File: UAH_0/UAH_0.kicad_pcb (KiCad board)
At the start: 2 copper layers, 100 x 100 mm, 30 parts, among them X1 Check_point, X2 Check_point, X3 LOGO_NIKITOS_19х7, X5 Клеммник_х2_KLS2-300-5.00-02P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

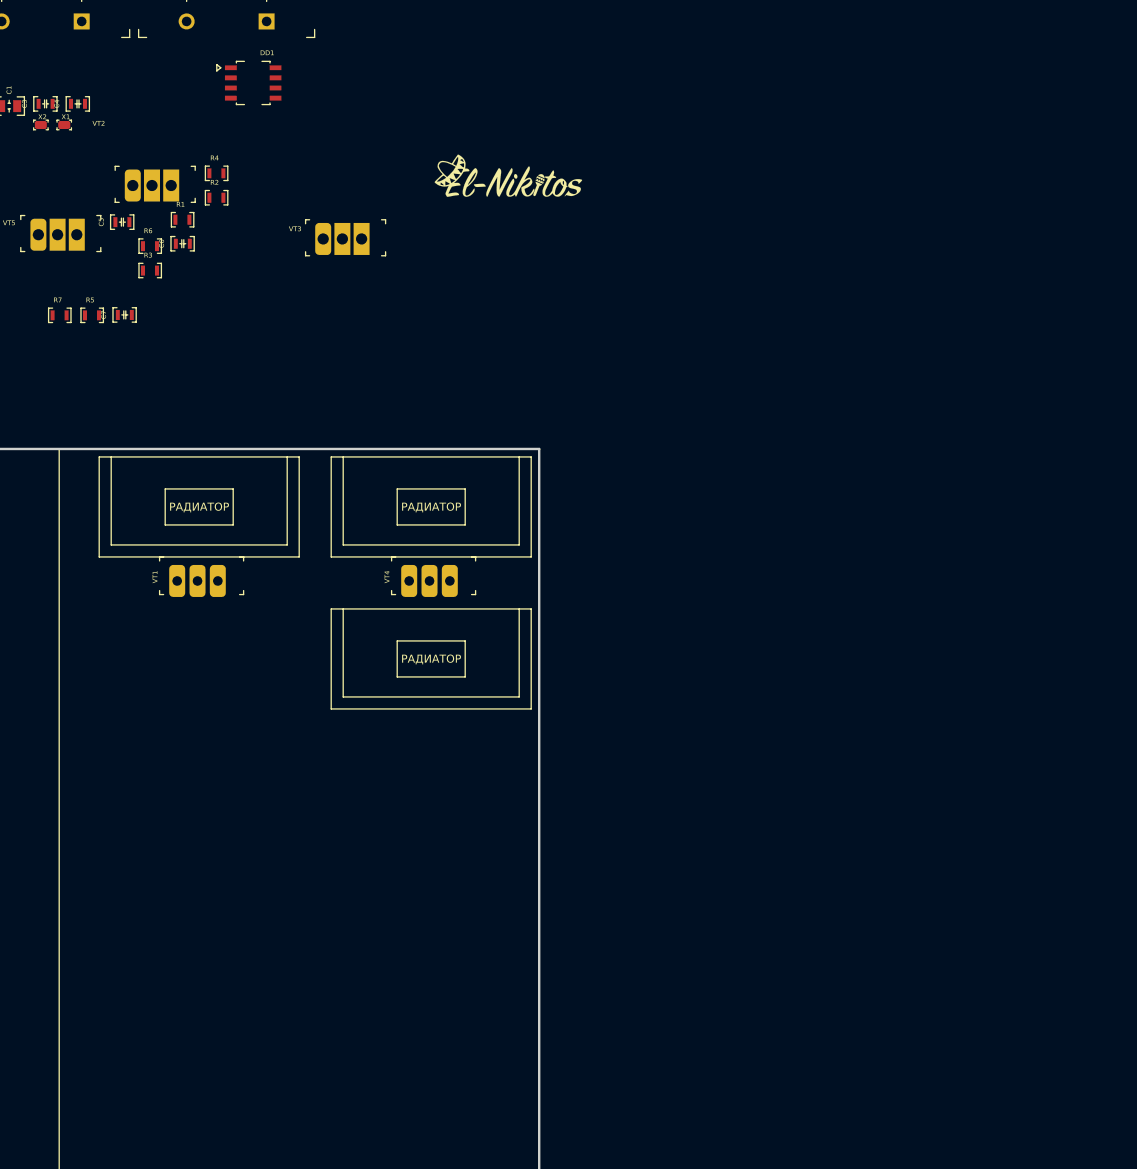
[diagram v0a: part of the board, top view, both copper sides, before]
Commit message: обновлена схема управления движками
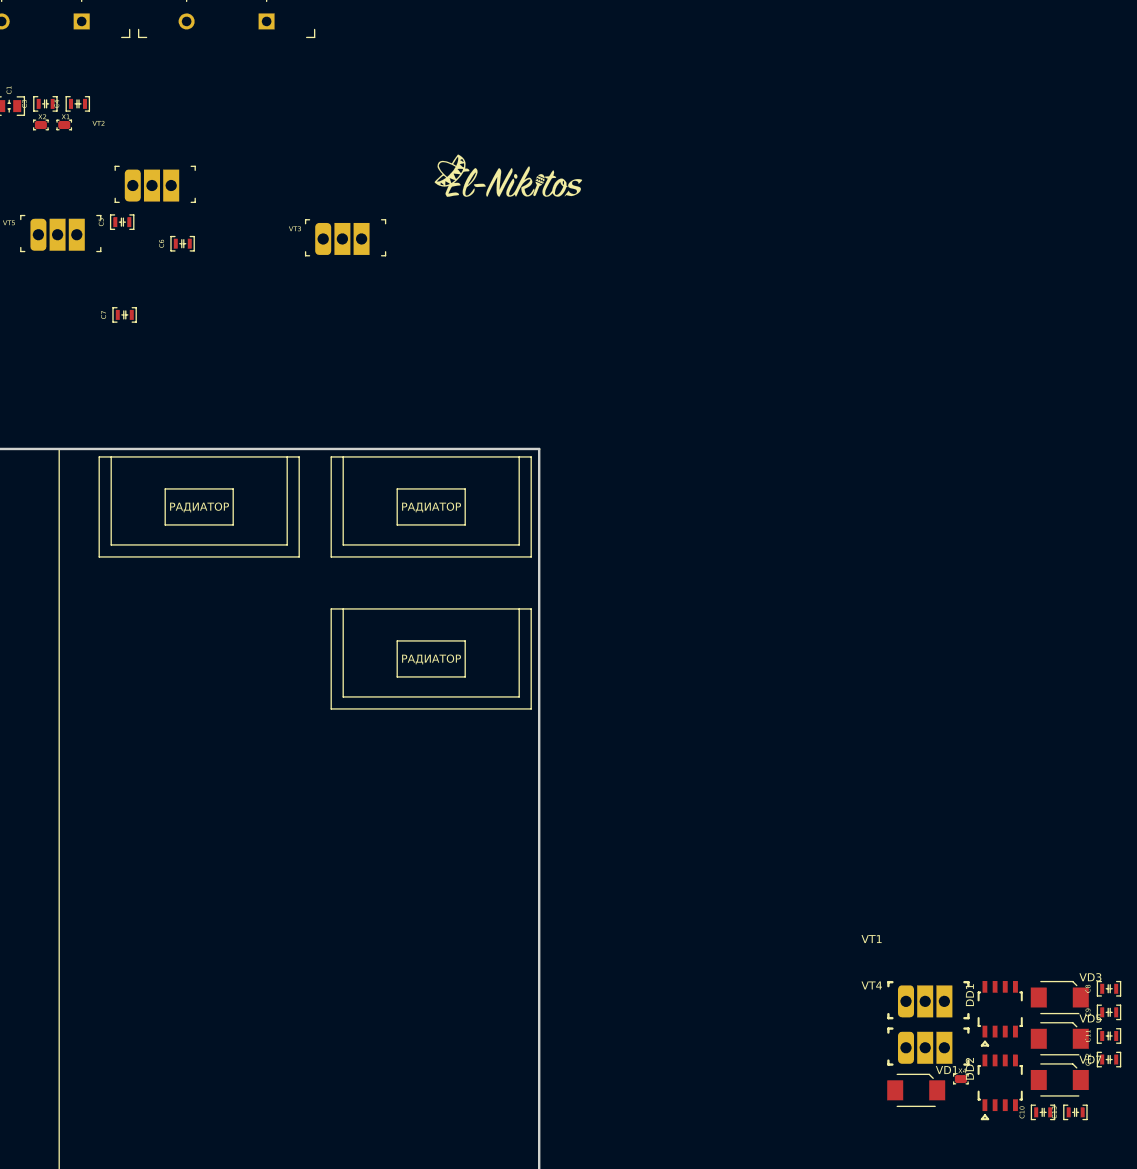
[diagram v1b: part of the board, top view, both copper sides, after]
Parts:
- removed R1, R2, R6, R7: Резистор_10_кОм±5%_0,1Вт, MOTOR_RLC:Резистор_SMD_0603-0,075_Вт
- removed R3, R4, R5: Резистор_470_Ом±5%_0,1Вт, MOTOR_RLC:Резистор_SMD_0603-0,075_Вт
- added C10: Конденсатор_16В_0.1_мкФ+-10проц., MOTOR_RLC:Конденсатор_SMD_К10-83(0603), F.Cu at (212.1, 132.9)
- added C11: Конденсатор_16В_0.1_мкФ+-10проц., MOTOR_RLC:Конденсатор_SMD_К10-83(0603), F.Cu at (220.4, 123.4)
- added C12: Конденсатор_16В_0.1_мкФ+-10проц., MOTOR_RLC:Конденсатор_SMD_К10-83(0603), F.Cu at (220.4, 126.3)
- added C13: Конденсатор_16В_0.1_мкФ+-10проц., MOTOR_RLC:Конденсатор_SMD_К10-83(0603), F.Cu at (216.2, 132.9)
- added C8: Конденсатор_16В_0.1_мкФ+-10проц., MOTOR_RLC:Конденсатор_SMD_К10-83(0603), F.Cu at (220.4, 117.5)
- added C9: Конденсатор_16В_0.1_мкФ+-10проц., MOTOR_RLC:Конденсатор_SMD_К10-83(0603), F.Cu at (220.4, 120.4)
- added DD2: Драйвер_FET-IGBT_IR2103STRPBF, N_DD:SO-8, F.Cu at (207.6, 129.2)
- added VD1: Диод_шоттки_SK16, N_VD_HL:Диод_SMB, F.Cu at (194.8, 130.2)
- added VD3: Диод_шоттки_SK16, N_VD_HL:Диод_SMB, F.Cu at (212.7, 118.6)
- added VD5: Диод_шоттки_SK16, N_VD_HL:Диод_SMB, F.Cu at (212.7, 123.7)
- added VD7: Диод_шоттки_SK16, N_VD_HL:Диод_SMB, F.Cu at (212.7, 128.9)
- added X4: Check_point, N_X:Пробник, F.Cu at (202.7, 128.8)
- VT1, VT4: value MOSFET_P-канал_IRF4905PBF -> MOSFET_N-канал_AUIRF3205Z; footprint N_VD_HL:Транзистор_P_IRF9Z24NPBF -> N_VD_HL:Транзистор_N_STP10NK60Z
- moved DD1 148.7 mm to (207.6, 120.0), turned to 0 degrees
- moved VT1 105.2 mm to (195.9, 119.1)
- moved VT4 85.2 mm to (195.9, 124.9)
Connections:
- C5 pad 1: Net-(C5-Pad1) -> /PWR_COMMUTATION/12V
- C7 pad 1: Net-(C7-Pad1) -> /PWR_COMMUTATION/12V
- DD1 pad 1: Net-(DD1-Pad1) -> /PWR_COMMUTATION/15V
- DD1 pad 2: Net-(DD1-Pad2) -> /PWR_COMMUTATION/MODE_1
- DD1 pad 3: Net-(DD1-Pad3) -> /PWR_COMMUTATION/MODE_1
- DD1 pad 4: Net-(DD1-Pad4) -> /PWR_COMMUTATION/GND
- DD1 pad 5: Net-(DD1-Pad5) -> /PWR_COMMUTATION/MODE_1_L
- DD1 pad 6: Net-(DD1-Pad6) -> /PWR_COMMUTATION/OUT_2
- DD1 pad 7: Net-(DD1-Pad7) -> /PWR_COMMUTATION/MODE_1_H
- DD1 pad 8: Net-(DD1-Pad8) -> /PWR_COMMUTATION/VB
- VT1 pad 1: /PWR_COMMUTATION/MODE_1 -> /PWR_COMMUTATION/MODE_1_H
- VT1 pad 2: /PWR_COMMUTATION/OUT_2 -> /PWR_COMMUTATION/12V
- VT1 pad 3: /PWR_COMMUTATION/12V -> /PWR_COMMUTATION/OUT_2
- VT2 pad 1: /PWR_COMMUTATION/MODE_2 -> /PWR_COMMUTATION/MODE_2_L
- VT4 pad 1: /PWR_COMMUTATION/MODE_2 -> /PWR_COMMUTATION/MODE_2_H
- VT4 pad 2: /PWR_COMMUTATION/OUT_1 -> /PWR_COMMUTATION/12V
- VT4 pad 3: /PWR_COMMUTATION/12V -> /PWR_COMMUTATION/OUT_1
- VT5 pad 1: /PWR_COMMUTATION/MODE_1 -> /PWR_COMMUTATION/MODE_1_L

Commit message: закончена принципиальная схема, подготовлен мост и обвес на 1й канал
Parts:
- removed the VD3 at (212.7, 118.6)
- added C1: Конденсатор_16В_0.1_мкФ+-10проц., MOTOR_RLC:Конденсатор_SMD_К10-83(0603), F.Cu at (113.2, -41.0)
- added C12: Конденсатор_16В_0.1_мкФ+-10проц., MOTOR_RLC:Конденсатор_SMD_К10-83(0603), F.Cu at (197.4, 68.8)
- added C14: Конденсатор_16В_10_мкФ+-10проц., MOTOR_RLC:Конденсатор_SMD_0805, F.Cu at (65.8, -17.0)
- added C16: Конденсатор_16В_0.1_мкФ+-10проц., MOTOR_RLC:Конденсатор_SMD_К10-83(0603), F.Cu at (248.8, -2.50)
- added C17: Конденсатор_16В_0.1_мкФ+-10проц., MOTOR_RLC:Конденсатор_SMD_К10-83(0603), F.Cu at (65.5, -10.8)
- added C18: Конденсатор_16В_0.1_мкФ+-10проц., MOTOR_RLC:Конденсатор_SMD_К10-83(0603), F.Cu at (177.5, 91.5)
- added C19: Конденсатор_16В_0.1_мкФ+-10проц., MOTOR_RLC:Конденсатор_SMD_К10-83(0603), F.Cu at (167.5, 95.0)
- added C2: Конденсатор_16В_0.1_мкФ+-10проц., MOTOR_RLC:Конденсатор_SMD_К10-83(0603), F.Cu at (117.3, -41.0)
- added C24: Конденсатор_16В_0.1_мкФ+-10проц., MOTOR_RLC:Конденсатор_SMD_К10-83(0603), F.Cu at (266.8, 68.0)
- added C25: Конденсатор_16В_0.1_мкФ+-10проц., MOTOR_RLC:Конденсатор_SMD_К10-83(0603), F.Cu at (261.8, 72.4)
- added C26: Конденсатор_16В_0.1_мкФ+-10проц., MOTOR_RLC:Конденсатор_SMD_К10-83(0603), F.Cu at (270.8, 69.3)
- added C27: Конденсатор_16В_0.1_мкФ+-10проц., MOTOR_RLC:Конденсатор_SMD_К10-83(0603), F.Cu at (276.6, 62.9)
- added C28: Конденсатор_16В_0.1_мкФ+-10проц., MOTOR_RLC:Конденсатор_SMD_К10-83(0603), F.Cu at (266.8, 71.0)
- added C29: Конденсатор_16В_0.1_мкФ+-10проц., MOTOR_RLC:Конденсатор_SMD_К10-83(0603), F.Cu at (271.6, 66.3)
- added C30: Конденсатор_16В_0.1_мкФ+-10проц., MOTOR_RLC:Конденсатор_SMD_К10-83(0603), F.Cu at (270.8, 99.3)
- added C31: Конденсатор_16В_0.1_мкФ+-10проц., MOTOR_RLC:Конденсатор_SMD_К10-83(0603), F.Cu at (276.6, 92.9)
- added C32: Конденсатор_16В_0.1_мкФ+-10проц., MOTOR_RLC:Конденсатор_SMD_К10-83(0603), F.Cu at (266.8, 101.0)
- added C33: Конденсатор_16В_0.1_мкФ+-10проц., MOTOR_RLC:Конденсатор_SMD_К10-83(0603), F.Cu at (271.6, 96.4)
- added C34: Конденсатор_16В_0.1_мкФ+-10проц., MOTOR_RLC:Конденсатор_SMD_К10-83(0603), F.Cu at (266.8, 98.0)
- added C35: Конденсатор_16В_0.1_мкФ+-10проц., MOTOR_RLC:Конденсатор_SMD_К10-83(0603), F.Cu at (261.8, 102.4)
- added C5: Конденсатор_16В_0.1_мкФ+-10проц., MOTOR_RLC:Конденсатор_SMD_К10-83(0603), F.Cu at (113.2, -35.1)
- added C7: Конденсатор_К53-56А-32В-22_мкФ+-10проц., MOTOR_RLC:Конденсатор_тантал_SMD_m7343, F.Cu at (179.5, 70.2)
- added DA1: МОП-реле_КР293КП4_0, N_DD:DIP8, F.Cu at (189.4, -3.60)
- added DA2: МОП-реле_КР293КП4_0, N_DD:DIP8, F.Cu at (234.5, 51.5)
- added DA3: МОП-реле_КР293КП4_0, N_DD:DIP8, F.Cu at (234.5, 81.5)
- added FU1: 30А_6.35х30, N_RLC:Предохранитель_6.35x30, F.Cu at (20.2, 18.5)
- added G1: AC-DC-преобразователь_IRM-10-15, N_G:AC-DC_IRM-10-15, F.Cu at (-48.2, 52.5)
- added R1: Резистор_Р1-12-0,1_ум.-240_Ом±5%-Н-«А», MOTOR_RLC:Резистор_SMD_0603-0,075_Вт, F.Cu at (117.2, -35.0)
- added R10: Резистор_Р1-12-0,125-270_Ом±5%-Н-«А», MOTOR_RLC:Резистор_SMD_0805_0,125Вт, F.Cu at (172.8, 91.8)
- added R11: Резистор_Р1-12-0,125-270_Ом±5%-Н-«А», MOTOR_RLC:Резистор_SMD_0805_0,125Вт, F.Cu at (167.8, 91.8)
- added R12: Резистор_CF-100_10_Ом_1Вт, N_RLC:резистор_C1-4-1_Вт_вертикальный, F.Cu at (66.5, 58.0)
- added R13: Резистор_Р1-12-0,125-270_Ом±5%-Н-«А», MOTOR_RLC:Резистор_SMD_0805_0,125Вт, F.Cu at (262.1, 69.2)
- added R14: Резистор_Р1-12-0,125-270_Ом±5%-Н-«А», MOTOR_RLC:Резистор_SMD_0805_0,125Вт, F.Cu at (272.0, 63.1)
- added R15: Резистор_CF-100_10_Ом_1Вт, N_RLC:резистор_C1-4-1_Вт_вертикальный, F.Cu at (178.3, 29.1)
- added R16: Резистор_Р1-12-0,125-270_Ом±5%-Н-«А», MOTOR_RLC:Резистор_SMD_0805_0,125Вт, F.Cu at (272.0, 93.1)
- added R17: Резистор_Р1-12-0,125-270_Ом±5%-Н-«А», MOTOR_RLC:Резистор_SMD_0805_0,125Вт, F.Cu at (262.1, 99.2)
- added R18: Резистор_CF-100_10_Ом_1Вт, N_RLC:резистор_C1-4-1_Вт_вертикальный, F.Cu at (205.0, 12.8)
- added R2: Резистор_Р1-12-0,1_ум.-240_Ом±5%-Н-«А», MOTOR_RLC:Резистор_SMD_0603-0,075_Вт, F.Cu at (113.2, -29.1)
- added R3: Резистор_Р1-12-0,1_ум.-240_Ом±5%-Н-«А», MOTOR_RLC:Резистор_SMD_0603-0,075_Вт, F.Cu at (117.2, -32.0)
- added R4: Резистор_Р1-12-0,1_ум.-240_Ом±5%-Н-«А», MOTOR_RLC:Резистор_SMD_0603-0,075_Вт, F.Cu at (113.2, -26.1)
- added R5: Резистор_Р1-12-0,1_ум.-240_Ом±5%-Н-«А», MOTOR_RLC:Резистор_SMD_0603-0,075_Вт, F.Cu at (117.2, -28.9)
- added R6: Резистор_Р1-12-0,1_ум.-240_Ом±5%-Н-«А», MOTOR_RLC:Резистор_SMD_0603-0,075_Вт, F.Cu at (117.2, -25.9)
- added R7: Резистор_CF-100_10_Ом_1Вт, N_RLC:резистор_C1-4-1_Вт_вертикальный, F.Cu at (195.2, 29.1)
- added R8: Резистор_10_кОм±5%_0,1Вт, MOTOR_RLC:Резистор_SMD_0603-0,075_Вт, F.Cu at (123.5, 29.7)
- added R9: Резистор_10_кОм±5%_0,1Вт, MOTOR_RLC:Резистор_SMD_0603-0,075_Вт, F.Cu at (127.6, 26.8)
- added VD10: Диод_шоттки_SK16, N_VD_HL:Диод_SMB, F.Cu at (254.1, 70.0)
- added VD11: Стабилитрон_1N5352BRLG_вертикальный, N_VD_HL:стабилитрон_DO-201_вертикальный, F.Cu at (168.5, 35.2)
- added VD12: Диод_VS-20ETS08S-M3, N_VD_HL:Транзистор_N-канал_dpak, F.Cu at (248.3, 86.5)
- added VD13: Диод_шоттки_SK16, N_VD_HL:Диод_SMB, F.Cu at (254.1, 100.0)
- added VD14: Стабилитрон_1N5352BRLG_вертикальный, N_VD_HL:стабилитрон_DO-201_вертикальный, F.Cu at (195.2, 12.8)
- added VD15: Диод_шоттки_SK16, N_VD_HL:Диод_SMB, F.Cu at (264.0, 94.0)
- added VD16: Стабилитрон_1N5352BRLG_вертикальный, N_VD_HL:стабилитрон_DO-201_вертикальный, F.Cu at (195.2, 18.9)
- added VD4: Стабилитрон_1N5352BRLG_вертикальный, N_VD_HL:стабилитрон_DO-201_вертикальный, F.Cu at (54.8, 54.0)
- added VD6: Стабилитрон_1N5352BRLG_вертикальный, N_VD_HL:стабилитрон_DO-201_вертикальный, F.Cu at (61.0, 58.0)
- added VD7: Диод_VS-20ETS08S-M3, N_VD_HL:Транзистор_N-канал_dpak, F.Cu at (248.3, 56.5)
- added VD8: Диод_шоттки_SK16, N_VD_HL:Диод_SMB, F.Cu at (264.0, 64.0)
- added VD9: Стабилитрон_1N5352BRLG_вертикальный, N_VD_HL:стабилитрон_DO-201_вертикальный, F.Cu at (168.5, 29.1)
- added VT10: MOSFET_N-канал_STD60N3LH5, N_VD_HL:IGBT_dpak, F.Cu at (256.6, 56.1)
- added VT11: MOSFET_N-канал_STD60N3LH5, N_VD_HL:IGBT_dpak, F.Cu at (272.9, 86.2)
- added VT12: MOSFET_N-канал_STD60N3LH5, N_VD_HL:IGBT_dpak, F.Cu at (248.2, 99.5)
- added VT13: MOSFET_N-канал_STD60N3LH5, N_VD_HL:IGBT_dpak, F.Cu at (256.6, 86.2)
- added VT14: MOSFET_N-канал_STD60N3LH5, N_VD_HL:IGBT_dpak, F.Cu at (264.7, 86.2)
- added VT6: MOSFET_N-канал_STD60N3LH5, N_VD_HL:IGBT_dpak, F.Cu at (71.0, 71.2)
- added VT7: MOSFET_N-канал_STD60N3LH5, N_VD_HL:IGBT_dpak, F.Cu at (248.2, 69.5)
- added VT8: MOSFET_N-канал_STD60N3LH5, N_VD_HL:IGBT_dpak, F.Cu at (272.9, 56.1)
- added VT9: MOSFET_N-канал_STD60N3LH5, N_VD_HL:IGBT_dpak, F.Cu at (264.7, 56.1)
- added X10: Check_point, N_X:Пробник, F.Cu at (64.8, 45.4)
- added X11: Check_point, N_X:Пробник, F.Cu at (67.7, 45.4)
- added X12: Check_point, N_X:Пробник, F.Cu at (73.7, 39.0)
- added X13: Check_point, N_X:Пробник, F.Cu at (76.6, 39.0)
- added X5: Крепежное_отверстие_М3, MOTOR_ICO:Крепежное_Отверстие_под_М3, F.Cu at (259.6, -5.78)
- added X6: Крепежное_отверстие_М3, MOTOR_ICO:Крепежное_Отверстие_под_М3, F.Cu at (267.6, -5.78)
- added X7: LOGO_NIKITOS_19х7, N_ICO:el-nikitos_19x7, F.Cu at (143.2, -5.50)
- added X8: Check_point, N_X:Пробник, F.Cu at (74.0, 62.5)
- added X9: Check_point, N_X:Пробник, F.Cu at (89.5, 62.5)
- added XT10: Клеммник_х2_KLS2-300-5.00-02P-2S, N_X:Клеммник_х2_шаг5, F.Cu at (89.2, 54.5)
- added XT11: Клеммник_х2_KLS2-300-5.00-02P-2S, N_X:Клеммник_х2_шаг5, F.Cu at (182.1, 62.8)
- added XT12: Клеммник_х2_KLS2-300-5.00-02P-2S, N_X:Клеммник_х2_шаг5, F.Cu at (182.1, 53.0)
- added XT13: Клеммник_х2_KLS2-300-5.00-02P-2S, N_X:Клеммник_х2_шаг5, F.Cu at (169.9, 62.8)
- added XT14: Клеммник_х2_KLS2-300-5.00-02P-2S, N_X:Клеммник_х2_шаг5, F.Cu at (169.9, 53.0)
- added XT15: Клеммник_х2_KLS2-300-5.00-02P-2S, N_X:Клеммник_х2_шаг5, F.Cu at (239.0, -12.7)
- added XT16: Клеммник_х2_KLS2-300-5.00-02P-2S, N_X:Клеммник_х2_шаг5, F.Cu at (239.0, -2.98)
- added XT4: Клеммник_х2_KLS2-300-5.00-02P-2S, N_X:Клеммник_х2_шаг5, F.Cu at (91.3, -37.4)
- added XT5: Клеммник_х2_KLS2-300-5.00-02P-2S, N_X:Клеммник_х2_шаг5, F.Cu at (55.7, -13.6)
- added XT6: Клеммник_х2_KLS2-300-5.00-02P-2S, N_X:Клеммник_х2_шаг5, F.Cu at (91.3, -27.7)
- added XT7: Клеммник_х2_KLS2-300-5.00-02P-2S, N_X:Клеммник_х2_шаг5, F.Cu at (103.5, -37.4)
- added XT8: Клеммник_х2_KLS2-300-5.00-02P-2S, N_X:Клеммник_х2_шаг5, F.Cu at (103.5, -27.7)
- added XT9: Клеммник_х2_KLS2-300-5.00-02P-2S, N_X:Клеммник_х2_шаг5, F.Cu at (79.2, 54.5)
- C8: value Конденсатор_16В_0.1_мкФ+-10проц. -> Конденсатор_16В_10_мкФ+-10проц.; footprint MOTOR_RLC:Конденсатор_SMD_К10-83(0603) -> MOTOR_RLC:Конденсатор_SMD_0805
- VD1: value Диод_шоттки_SK16 -> Стабилитрон_1N5352BRLG_вертикальный; footprint N_VD_HL:Диод_SMB -> N_VD_HL:стабилитрон_DO-201_вертикальный
- VD3: renamed from VD5; moved to B.Cu
- VD5: renamed from VD7; moved to B.Cu
- VT3, VT4, VT5: value MOSFET_N-канал_AUIRF3205Z -> MOSFET_N-канал_STD60N3LH5; footprint N_VD_HL:Транзистор_N_STP10NK60Z -> N_VD_HL:IGBT_dpak
- X3: value LOGO_NIKITOS_19х7 -> Крепежное_отверстие_М3; footprint N_ICO:el-nikitos_19x7 -> MOTOR_ICO:Крепежное_Отверстие_под_М3
- X4: value Check_point -> Крепежное_отверстие_М3; footprint N_X:Пробник -> MOTOR_ICO:Крепежное_Отверстие_под_М3
- moved VD1 206.9 mm to (35.8, -2.25)
- moved C11 206.9 mm to (65.5, -13.8)
- moved VD3 160.9 mm to (61.2, 69.5)
- moved VD5 160.4 mm to (66.0, 64.0), turned to 180 degrees
- moved X4 154.7 mm to (262.9, -13.8)
- moved VT2 154.5 mm to (250.4, -14.7)
- moved C10 138.3 mm to (123.6, 26.7)
- moved DD2 133.5 mm to (119.1, 29.3)
- moved VT4 116.2 mm to (92.8, 71.2), turned to 180 degrees
- moved X3 107.8 mm to (251.6, -7.98)
- moved A1 85.4 mm to (-22.8, 89.0)
- moved VT3 69.2 mm to (92.8, 86.0), turned to 180 degrees
- moved DD1 68.1 mm to (206.2, 52.0)
- moved VT5 64.9 mm to (71.0, 86.0), turned to 180 degrees
- moved C9 62.8 mm to (209.1, 58.6)
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- renumbered C1 to C13, C2 to C15, C5 to C20, C12 to C21, C7 to C22, C13 to C23, X5 to XT3
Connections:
- net /PWR_COMMUTATION/MODE_1 renamed /DRIVE_MC_1
- net /PWR_COMMUTATION/MODE_2 renamed /DRIVE_MC_2
- A1 pad 1: Net-(A1-Pad1) -> /12V_MC
- A1 pad 14: Net-(A1-Pad14) -> /3V3
- A1 pad 19: Net-(A1-Pad19) -> /0(12V)_MC
- A1 pad 2: Net-(A1-Pad2) -> /0(12V)_MC
- A1 pad 4: Net-(A1-Pad4) -> /5V_MC
- C10 pad 1: /PWR_COMMUTATION/VB -> /15V_MOSFET
- C10 pad 2: /PWR_COMMUTATION/OUT_2 -> /0(12V)_MC
- C11 pad 1: /PWR_COMMUTATION/VB -> /3V3
- C11 pad 2: /PWR_COMMUTATION/OUT_1 -> /0(12V)_MC
- C20 pad 1: /PWR_COMMUTATION/12V -> /12V_FU
- C20 pad 2: /PWR_COMMUTATION/OUT_2 -> /OUT_1_2
- C21 pad 1: /PWR_COMMUTATION/OUT_2 -> /OUT_1_2
- C21 pad 2: Net-(C12-Pad2) -> /PWR_COMMON
- C22 pad 1: /PWR_COMMUTATION/12V -> /12V_FU
- C22 pad 2: /PWR_COMMUTATION/OUT_1 -> /OUT_1_1
- C23 pad 1: /PWR_COMMUTATION/OUT_1 -> /OUT_1_1
- C23 pad 2: Net-(C12-Pad2) -> /PWR_COMMON
- C3 pad 1: /15V_MOSFET -> /MC_DIN_6
- C3 pad 2: Net-(C3-Pad2) -> /0(12V)_MC
- C4 pad 1: Net-(C4-Pad1) -> /MC_DIN_1
- C4 pad 2: /15V_MOSFET -> /0(12V)_MC
- C6 pad 1: Net-(C6-Pad1) -> /MC_DIN_5
- C6 pad 2: /PWR_COMMUTATION/0(12V) -> /0(12V)_MC
- C8 pad 1: /PWR_COMMUTATION/15V -> /15V_MOSFET
- C8 pad 2: /PWR_COMMUTATION/GND -> /0(12V)_MC
- C9 pad 1: /PWR_COMMUTATION/15V -> /15V_MOSFET
- C9 pad 2: /PWR_COMMUTATION/GND -> /0(12V)_MC
- DD1 pad 1: /PWR_COMMUTATION/15V -> /15V_MOSFET
- DD1 pad 4: /PWR_COMMUTATION/GND -> /0(12V)_MC
- DD1 pad 5: /PWR_COMMUTATION/MODE_1_L -> /DRIVE_1
- DD1 pad 6: /PWR_COMMUTATION/OUT_2 -> Net-(DD1-Pad6)
- DD1 pad 7: /PWR_COMMUTATION/MODE_1_H -> Net-(DD1-Pad7)
- DD1 pad 8: /PWR_COMMUTATION/VB -> Net-(DD1-Pad8)
- DD2 pad 1: /PWR_COMMUTATION/15V -> /15V_MOSFET
- DD2 pad 4: /PWR_COMMUTATION/GND -> /0(12V)_MC
- DD2 pad 5: /PWR_COMMUTATION/MODE_2_L -> /DRIVE_2
- DD2 pad 6: /PWR_COMMUTATION/OUT_1 -> Net-(DD2-Pad6)
- DD2 pad 7: /PWR_COMMUTATION/MODE_2_H -> Net-(DD2-Pad7)
- DD2 pad 8: /PWR_COMMUTATION/VB -> Net-(DD2-Pad8)
- L1 pad 1: Net-(L1-Pad1) -> /15V_MOSFET
- L1 pad 3: Net-(L1-Pad3) -> /0(12V)_MC
- VD1 pad 1: /PWR_COMMUTATION/15V -> Net-(C12-Pad1)
- VD1 pad 2: /PWR_COMMUTATION/VB -> /PWR_COMMON
- VD2 pad 1: Net-(C12-Pad2) -> /PWR_COMMON
- VD2 pad 2: /PWR_COMMUTATION/12V -> /12V_FU
- VD2 pad 3: Net-(C12-Pad2) -> /PWR_COMMON
- VD3 pad 2: /PWR_COMMUTATION/OUT_1 -> Net-(VD3-Pad2)
- VD5 pad 1: /PWR_COMMUTATION/OUT_1 -> Net-(VD3-Pad2)
- VT1 pad 1: /PWR_COMMUTATION/MODE_1_H -> /DRIVE_1
- VT1 pad 2: /PWR_COMMUTATION/12V -> /PWR_COMMON
- VT1 pad 3: /PWR_COMMUTATION/OUT_2 -> /0(12V)_IN
- VT2 pad 1: /PWR_COMMUTATION/MODE_2_L -> /DRIVE_1
- VT2 pad 2: /PWR_COMMUTATION/OUT_2 -> /HEAT_OK
- VT2 pad 3: Net-(C12-Pad2) -> /0(12V)_IN
- VT3 pad 1: /PWR_COMMUTATION/CONTROL -> /PWR_COMMUTATION_1/CHANNEL_1
- VT3 pad 3: /PWR_COMMUTATION/0(12V) -> /OUT_1_2
- VT4 pad 1: /PWR_COMMUTATION/MODE_2_H -> /PWR_COMMUTATION_1/CHANNEL_2
- VT4 pad 3: /PWR_COMMUTATION/OUT_1 -> /PWR_COMMON
- VT5 pad 1: /PWR_COMMUTATION/MODE_1_L -> /PWR_COMMUTATION_1/CHANNEL_2
- VT5 pad 3: Net-(C12-Pad2) -> /OUT_1_1
- X4 pad 1: /PWR_COMMUTATION/GND -> Net-(X4-Pad1)
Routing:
- net /OUT_1_1: track 0.00 -> 31.2 mm
- net Net-(R12-Pad2): track 0.00 -> 29.9 mm, vias 0 -> 1
- net Net-(VD3-Pad1): track 0.00 -> 20.3 mm
- net /OUT_1_2: track 0.00 -> 17.2 mm
- net Net-(VD5-Pad2): track 0.00 -> 15.4 mm
- net Net-(VD3-Pad2): track 0.00 -> 15.0 mm, vias 0 -> 1
- net Net-(R12-Pad1): track 0.00 -> 12.2 mm
- added copper zone on F.Cu, net /12V_FU
- added copper zone on F.Cu, net /OUT_1_1
- added copper zone on F.Cu, net /OUT_1_2
- added copper zone on F.Cu, net /PWR_COMMON
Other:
- net class 20A_MAX: trace_width 6 -> 4.5

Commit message: расставлена силовая часть на 3 канала, нет управления и главных ключей
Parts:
- removed A1: модуль_arduino_nano, N_A:Arduino_nano
- removed VD12, VD7: Диод_VS-20ETS08S-M3, N_VD_HL:Транзистор_N-канал_dpak
- added R19: Резистор_10_кОм±5%_0,1Вт, MOTOR_RLC:Резистор_SMD_0603-0,075_Вт, F.Cu at (133.0, -38.2)
- added R20: Резистор_10_кОм±5%_0,1Вт, MOTOR_RLC:Резистор_SMD_0603-0,075_Вт, F.Cu at (137.1, -38.2)
- added R21: Резистор_10_кОм±5%_0,1Вт, MOTOR_RLC:Резистор_SMD_0603-0,075_Вт, F.Cu at (133.0, -29.6)
- added R22: Резистор_10_кОм±5%_0,1Вт, MOTOR_RLC:Резистор_SMD_0603-0,075_Вт, F.Cu at (137.1, -29.6)
- added R23: Резистор_10_кОм±5%_0,1Вт, MOTOR_RLC:Резистор_SMD_0603-0,075_Вт, F.Cu at (146.0, -38.2)
- added R24: Резистор_10_кОм±5%_0,1Вт, MOTOR_RLC:Резистор_SMD_0603-0,075_Вт, F.Cu at (150.0, -38.2)
- added X14: Check_point, N_X:Пробник, F.Cu at (133.3, -35.6)
- added X15: Check_point, N_X:Пробник, F.Cu at (133.3, -27.0)
- added X16: Check_point, N_X:Пробник, F.Cu at (146.3, -35.6)
- VD10, VD13, VD15, VD8: moved to B.Cu
- VT1, VT2: footprint N_VD_HL:Транзистор_N_STP10NK60Z -> N_VD_HL:Транзистор_TO-220_COOLING
- moved X3 249.1 mm to (55.0, 145.0)
- moved X5 213.4 mm to (55.0, 55.0)
- moved X6 156.7 mm to (225.0, 145.0)
- moved VD8 152.6 mm to (111.5, 69.5)
- moved VT9 146.5 mm to (121.2, 86.0), turned to 180 degrees
- moved VD10 138.0 mm to (116.2, 64.0), turned to 180 degrees
- moved VT10 136.1 mm to (121.2, 71.2), turned to 180 degrees
- moved C18 131.0 mm to (175.7, -39.5)
- moved C19 131.0 mm to (165.7, -36.0)
- moved C21 131.0 mm to (218.6, -4.67)
- moved C23 131.0 mm to (214.4, 1.93)
- moved C30 131.0 mm to (269.1, -31.7)
- moved C31 131.0 mm to (274.9, -38.1)
- moved C32 131.0 mm to (265.0, -30.0)
- moved C33 131.0 mm to (269.9, -34.6)
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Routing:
- net /OUT_3_1: track 0.00 -> 31.2 mm
- net /OUT_2_1: track 0.00 -> 31.2 mm
- net Net-(R18-Pad2): track 0.00 -> 29.9 mm, vias 0 -> 1
- net Net-(R15-Pad2): track 0.00 -> 29.9 mm, vias 0 -> 1
- net Net-(VD8-Pad1): track 0.00 -> 20.3 mm
- net Net-(VD13-Pad1): track 0.00 -> 20.3 mm
- net /OUT_3_2: track 0.00 -> 17.2 mm
- net /OUT_2_2: track 0.00 -> 17.2 mm
- net Net-(VD15-Pad2): track 0.00 -> 15.4 mm
- net Net-(VD10-Pad2): track 0.00 -> 15.4 mm
- net Net-(VD13-Pad2): track 0.00 -> 15.0 mm, vias 0 -> 1
- net Net-(VD10-Pad1): track 0.00 -> 15.0 mm, vias 0 -> 1
- net Net-(R18-Pad1): track 0.00 -> 12.2 mm
- net Net-(R15-Pad1): track 0.00 -> 12.2 mm
- net /PWR_COMMON: vias 0 -> 40
- added copper zone on F.Cu, net /0(12V)_IN
- added copper zone on F.Cu, net /12V_IN
- added copper zone on F.Cu, net /OUT_2_1
- added copper zone on F.Cu, net /OUT_2_2
- added copper zone on F.Cu, net /OUT_3_1
- added copper zone on F.Cu, net /OUT_3_2
- added copper zone on B.Cu, net /PWR_COMMON
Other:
- board size 100 x 100 mm -> 180 x 100 mm
- net class 20A_MAX: via_dia 0.8 -> 1.2; via_drill 0.4 -> 0.8
- board text removed: "РАДИАТОР"

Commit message: не подведены управления DI, габарит определен
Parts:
- removed C17, C20, C21, C22, C23, C26, C27, C28, C29, C32, C33, C34, C35: Конденсатор_16В_0.1_мкФ+-10проц., MOTOR_RLC:Конденсатор_SMD_К10-83(0603)
- removed L2: Дроссель_B82731-T2451-A20_2х47мГн_0.45А_250В, N_RLC:Дроссель_B82731
- removed X1, X14, X15, X16: Check_point, N_X:Пробник
- added A1: модуль_arduino_nano, N_A:Arduino_nano, F.Cu at (235.0, 135.0)
- added C36: Конденсатор_0.022мкФ_10проц_630В_1210, MOTOR_RLC:Конденсатор_SMD_1210, B.Cu at (207.2, 140.0)
- added FU2: Предохранитель_MF-MSMF010_0,1А_1812, N_RLC:Предохранитель_SMD_1812, F.Cu at (115.0, 146.8)
- added G2: стабилизатор_нерегулируемый_LM1117GS-5.0, N_VD_HL:Транзистор_NPN_SOT223, B.Cu at (189.8, 117.5)
- added R25: Резистор_Р1-12-0,125-120_Ом±5%-Н-«А», MOTOR_RLC:Резистор_SMD_0805_0,125Вт, B.Cu at (136.0, 119.8)
- added R26: Резистор_Р1-12-0,125-120_Ом±5%-Н-«А», MOTOR_RLC:Резистор_SMD_0805_0,125Вт, B.Cu at (153.2, 119.8)
- added X17: Check_point, N_X:Пробник, F.Cu at (144.2, 105.0)
- added X18: Check_point, N_X:Пробник, F.Cu at (144.2, 111.5)
- C1, C10, C11, C12, C13, C15, C16, C18, C19, C2, C24, C25, C3, C30, C31, C4, C5, C6, C7, C8, C9, DD1, DD2, R1, R10, R11, R13, R14, R16, R17, R19, R2, R20, R21, R22, R23, R24, R3, R4, R5, R6, R8, R9, X2: moved to B.Cu
- C14: footprint MOTOR_RLC:Конденсатор_SMD_0805 -> MOTOR_RLC:Конденсатор_SMD_К10-83(0603); moved to B.Cu
- XT4, XT5, XT6, XT7, XT8: footprint N_X:Клеммник_х2_шаг5 -> N_X:Клеммник_х2_шаг2.54
- moved G1 240.0 mm to (210.8, 145.0), turned to 90 degrees
- moved XT16 229.9 mm to (63.5, 145.5)
- moved XT15 226.4 mm to (77.0, 145.5)
- moved C11 221.0 mm to (232.2, 131.2), turned to 90 degrees
- moved XT5 208.5 mm to (235.8, 91.5), turned to 90 degrees
- moved C14 206.6 mm to (232.0, 105.8), turned to 90 degrees
- moved XT4 189.5 mm to (235.8, 85.3), turned to 90 degrees
- moved C1 180.0 mm to (227.2, 98.2), turned to 270 degrees
- moved C4 179.2 mm to (228.5, 102.5), turned to 270 degrees
- moved XT6 178.3 mm to (235.8, 76.8), turned to 90 degrees
- moved C5 176.3 mm to (223.5, 102.5), turned to 270 degrees
- moved C3 176.1 mm to (224.8, 98.2), turned to 270 degrees
- moved C6 175.6 mm to (226.0, 102.5), turned to 270 degrees
- moved C2 174.4 mm to (222.2, 98.2), turned to 270 degrees
- moved XT7 166.8 mm to (235.8, 64.2), turned to 90 degrees
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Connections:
- C12 pad 2: /0(12V)_IN -> Net-(C12-Pad2)
- C13 pad 1: Net-(C13-Pad1) -> /15V_MOSFET
- C13 pad 2: Net-(C13-Pad2) -> /0(12V)_MC
- C15 pad 1: /12V_MC -> /5V_MC
- C8 pad 1: /15V_MOSFET -> Net-(C8-Pad1)
- C8 pad 2: /0(12V)_MC -> Net-(C8-Pad2)
- DA1 pad 6: /PWR_COMMUTATION_1/CHANNEL_2 -> /PWR_COMMUTATION_1/CHANNEL_1
- DA1 pad 7: /PWR_COMMUTATION_1/CHANNEL_1 -> /PWR_COMMUTATION_1/CHANNEL_2
- DA2 pad 6: /PWR_COMMUTATION_2/CHANNEL_2 -> /PWR_COMMUTATION_2/CHANNEL_1
- DA2 pad 7: /PWR_COMMUTATION_2/CHANNEL_1 -> /PWR_COMMUTATION_2/CHANNEL_2
- DA3 pad 6: /sheet5F495C51/CHANNEL_2 -> /sheet5F495C51/CHANNEL_1
- DA3 pad 7: /sheet5F495C51/CHANNEL_1 -> /sheet5F495C51/CHANNEL_2
- G1 pad +V: Net-(G1-Pad+V) -> Net-(C8-Pad1)
- G1 pad -V: Net-(G1-Pad-V) -> Net-(C8-Pad2)
- G1 pad L: /220_L -> Net-(C36-Pad1)
- L1 pad 1: /15V_MOSFET -> Net-(C8-Pad1)
- L1 pad 3: /0(12V)_MC -> Net-(C8-Pad2)
- L1 pad 4: Net-(G1-Pad-V) -> /0(12V)_MC
- L1 pad 6: Net-(G1-Pad+V) -> /15V_MOSFET
- R10 pad 2: Net-(DA1-Pad2) -> Net-(DA1-Pad3)
- R11 pad 2: Net-(DA1-Pad3) -> Net-(DA1-Pad2)
- R13 pad 2: Net-(DA2-Pad2) -> Net-(DA2-Pad3)
- R14 pad 2: Net-(DA2-Pad3) -> Net-(DA2-Pad2)
- R16 pad 2: Net-(DA3-Pad2) -> Net-(DA3-Pad3)
- R17 pad 2: Net-(DA3-Pad3) -> Net-(DA3-Pad2)
- R19 pad 1: /PWR_COMMUTATION_1/PULL_DOWN -> /PWR_COMMON
- R20 pad 1: /PWR_COMMUTATION_1/PULL_DOWN -> /PWR_COMMON
- R21 pad 1: /PWR_COMMUTATION_2/PULL_DOWN -> /PWR_COMMON
- R22 pad 1: /PWR_COMMUTATION_2/PULL_DOWN -> /PWR_COMMON
- R23 pad 1: /sheet5F495C51/PULL_DOWN -> /PWR_COMMON
- R24 pad 1: /sheet5F495C51/PULL_DOWN -> /PWR_COMMON
- R7 pad 2: /0(12V)_IN -> Net-(C12-Pad2)
- VD1 pad 2: /PWR_COMMON -> Net-(VD1-Pad2)
- VT1 pad 1: /DRIVE_1 -> Net-(R25-Pad2)
- VT2 pad 1: /DRIVE_1 -> Net-(R26-Pad2)
- X2 pad 2: Net-(C13-Pad2) -> /0(12V)_MC
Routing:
- net /0(12V)_MC: track 0.00 -> 356.1 mm, vias 0 -> 6
- net /15V_MOSFET: track 0.00 -> 259.3 mm, vias 0 -> 5
- net /PWR_COMMUTATION_1/CHANNEL_2: track 0.00 -> 191.9 mm, vias 0 -> 3
- net /PWR_COMMUTATION_1/CHANNEL_1: track 0.00 -> 184.2 mm, vias 0 -> 5
- net /5V_MC: track 0.00 -> 153.7 mm
- net /PWR_COMMUTATION_2/CHANNEL_2: track 0.00 -> 134.5 mm, vias 0 -> 3
- net /PWR_COMMUTATION_2/CHANNEL_1: track 0.00 -> 130.6 mm, vias 0 -> 5
- net /220_N: track 0.00 -> 108.9 mm
- net Net-(C36-Pad1): track 0.00 -> 101.5 mm
- net /DRIVE_MC_1: track 0.00 -> 92.0 mm
- net /DRIVE_MC_2: track 0.00 -> 82.1 mm
- net /sheet5F495C51/CHANNEL_2: track 0.00 -> 80.9 mm, vias 0 -> 3
- net /sheet5F495C51/CHANNEL_1: track 0.00 -> 75.9 mm, vias 0 -> 5
- net /MC_DIN_3: track 0.00 -> 41.9 mm, vias 0 -> 2
- net /MC_DIN_4: track 0.00 -> 41.1 mm, vias 0 -> 2
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- added copper zone on F.Cu, net /0(12V)_MC
- added copper zone on F.Cu, net /HEAT_OK
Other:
- board size 180 x 100 mm -> 190 x 100 mm
- board text added: ".ru"
